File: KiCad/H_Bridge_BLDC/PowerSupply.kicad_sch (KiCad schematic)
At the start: 16 parts, among them J4 12V, Q10 BC33740BU, U2 L7805CV

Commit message: First version
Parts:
- removed C12: 470uF 250V, footprints:CP_Radial_D25.0mm_P10.00mm_and_5mm, symbol Components:470-uF-250V-PK2E471MND2535
- removed R22: 330, Resistor_THT:R_Axial_DIN0207_L6.3mm_D2.5mm_P10.16mm_Horizontal, symbol Device:R
- added D19: 20V 1N5250B, Diode_THT:D_DO-35_SOD27_P10.16mm_Horizontal, symbol Device:D_Zener
- added R12: 10k, Resistor_THT:R_Axial_DIN0207_L6.3mm_D2.5mm_P10.16mm_Horizontal, symbol Device:R
- added R13: 2k2, Resistor_THT:R_Axial_DIN0207_L6.3mm_D2.5mm_P10.16mm_Horizontal, symbol Device:R
- added R14: 1k, Resistor_THT:R_Axial_DIN0207_L6.3mm_D2.5mm_P10.16mm_Horizontal, symbol Device:R
- D18: value 24V / 2W -> ZY24 24V / 2W; footprint (none) -> Diode_THT:D_DO-41_SOD81_P10.16mm_Horizontal; Digikey (none) -> https://www.digikey.nl/short/zdt4nqp0
- Q10: value BC33740BU -> 2N5551; symbol Components:BC33740BU -> Components:2N5551; Digikey https://www.digikey.nl/short/0dchvj3v -> https://www.digikey.nl/short/t592041t
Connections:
- net GNDD: now also Q10.1 (E), R13.2; no longer Q10.3 (E)
- net HALL_ENABLE: now also D10.1 (K), Q10.3 (C); no longer Q10.1 (C)
- net VD: now also D19.1 (K), R12.1
- net at D10.2 (A): now also R12.2
- net at Q10.2 (B): now also R13.1, R14.2
- new net: D19.2 (A), R14.1
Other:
- note added: "Over Voltage detection"
- moved on the sheet: D10, FL1, R11, R40, R41

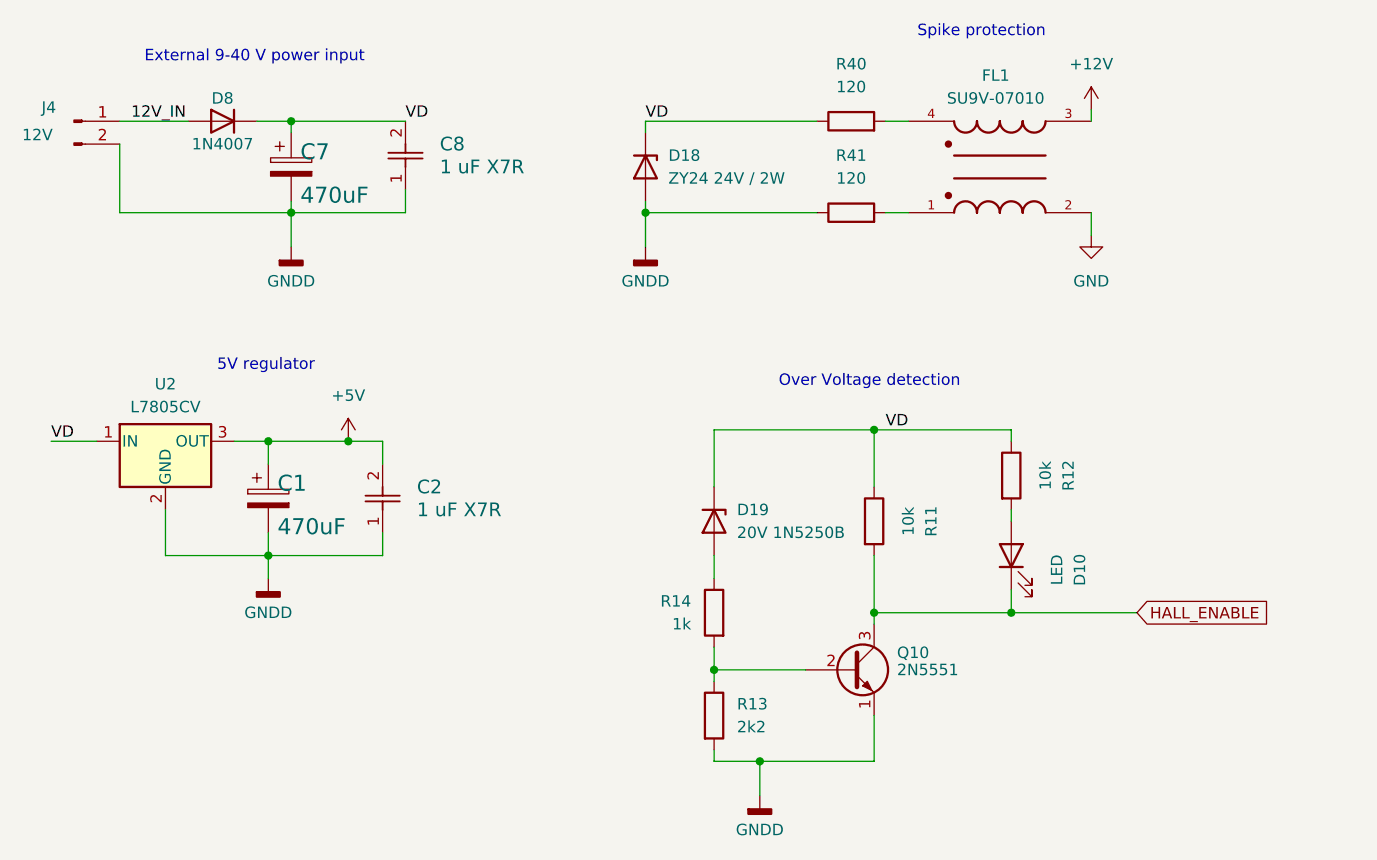
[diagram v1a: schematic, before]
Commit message: Added BOM and changed some parts (same footprint)
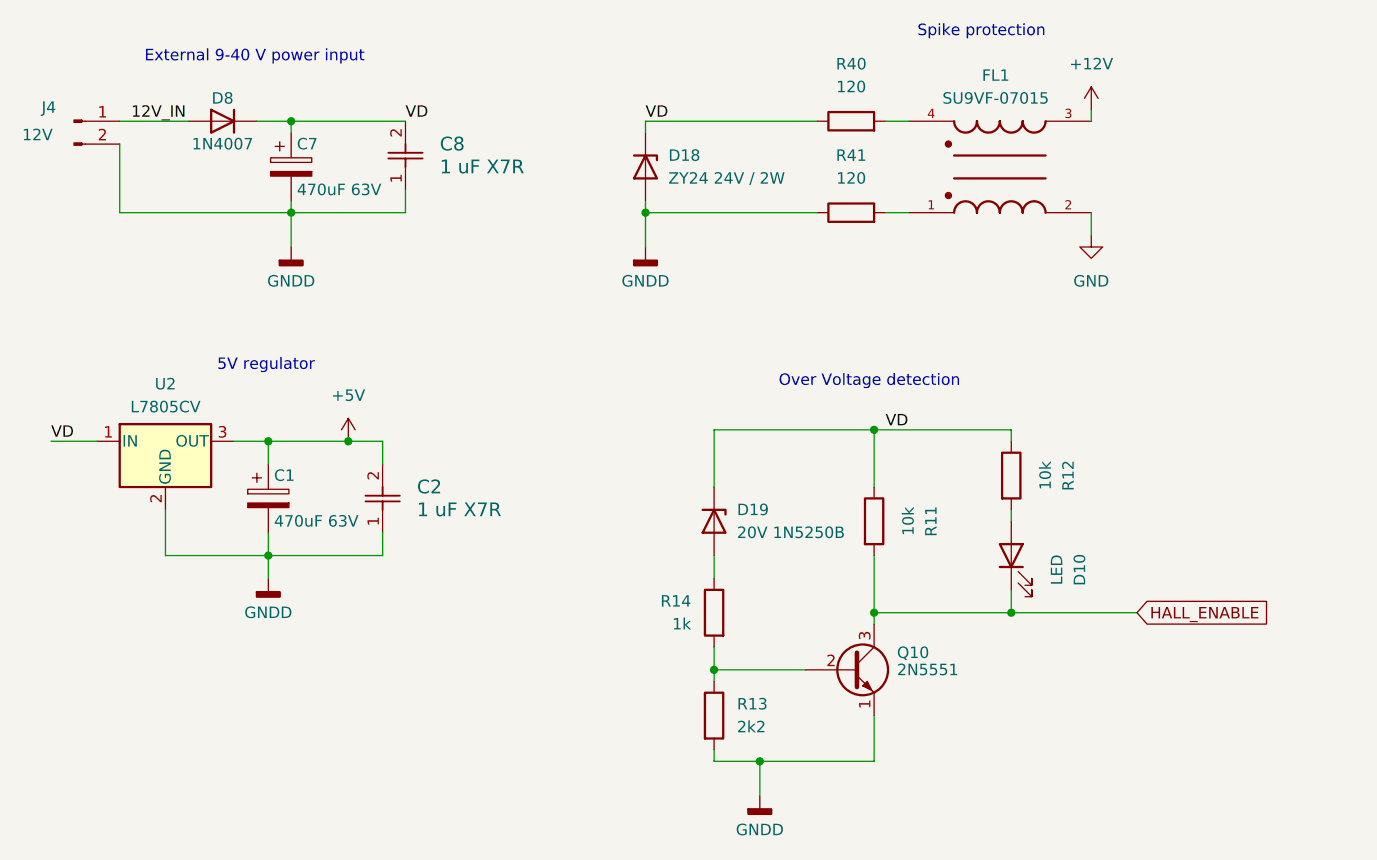
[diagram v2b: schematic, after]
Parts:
- C1, C7: value 470uF -> 470uF 63V; symbol Component_Library:C_Pol_470uF -> Components:470-uF-63V-ESK477M063AL4EA
- FL1: value SU9V-07010 -> SU9VF-07015; Digikey https://www.digikey.nl/short/fbcjc4v0 -> https://www.digikey.nl/short/8qzt38p9
- U2: DigiKey https://www.digikey.nl/short/7nprw4r0 -> (none); Digikey (none) -> https://www.digikey.nl/short/7nprw4r0
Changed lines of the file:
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@@
 			)
 		)
-		(property "Value" "SU9V-07010"
+		(property "Value" "SU9VF-07015"
 			(at 143.0528 41.91 0)
 			(effects
@@
 			)
 		)
-		(property "Description" "1 mH @ 1 kHz 2 Lijn Common Mode Choke Through-hole 700mA DCR 600mOhm"
+		(property "Description" "1.5 mH @ 1 kHz 2 Common Mode Choke Through-hole 700mA"
 			(at 143.51 49.53 0)
 			(effects
@@
 			)
 		)
-		(property "Digikey" "https://www.digikey.nl/short/fbcjc4v0"
+		(property "Digikey" "https://www.digikey.nl/short/8qzt38p9"
 			(at 143.51 49.53 0)
 			(effects
@@
 	)
 	(symbol
-		(lib_id "Component_Library:C_Pol_470uF")
+		(lib_id "Components:470-uF-63V-ESK477M063AL4EA")
 		(at 62.23 86.36 0)
 		(unit 1)
@@
 		(dnp no)
 		(property "Reference" "C1"
-			(at 63.246 85.725 0)
-			(effects
-				(font
-					(size 1.778 1.778)
-				)
-				(justify left bottom)
-			)
-		)
-		(property "Value" "470uF"
-			(at 63.246 90.551 0)
-			(effects
-				(font
-					(size 1.778 1.778)
-				)
-				(justify left bottom)
+			(at 62.865 83.82 0)
+			(effects
+				(font
+					(size 1.27 1.27)
+				)
+				(justify left)
+			)
+		)
+		(property "Value" "470uF 63V"
+			(at 62.865 88.9 0)
+			(effects
+				(font
+					(size 1.27 1.27)
+				)
+				(justify left)
 			)
 		)
@@
 			)
 		)
-		(property "Datasheet" "~"
+		(property "Datasheet" "https://search.kemet.com/download/datasheet/ESK477M063AL4EA"
 			(at 62.23 86.36 0)
 			(effects
@@
 	)
 	(symbol
-		(lib_id "Component_Library:C_Pol_470uF")
+		(lib_id "Components:470-uF-63V-ESK477M063AL4EA")
 		(at 64.77 49.53 0)
 		(unit 1)
@@
 		(dnp no)
 		(property "Reference" "C7"
-			(at 65.786 48.895 0)
-			(effects
-				(font
-					(size 1.778 1.778)
-				)
-				(justify left bottom)
-			)
-		)
-		(property "Value" "470uF"
-			(at 65.786 53.721 0)
-			(effects
-				(font
-					(size 1.778 1.778)
-				)
-				(justify left bottom)
+			(at 65.405 46.99 0)
+			(effects
+				(font
+					(size 1.27 1.27)
+				)
+				(justify left)
+			)
+		)
+		(property "Value" "470uF 63V"
+			(at 65.405 52.07 0)
+			(effects
+				(font
+					(size 1.27 1.27)
+				)
+				(justify left)
 			)
 		)
@@
 			)
 		)
-		(property "Datasheet" "~"
+		(property "Datasheet" "https://search.kemet.com/download/datasheet/ESK477M063AL4EA"
 			(at 64.77 49.53 0)
 			(effects
@@
 			)
 		)
-		(property "DigiKey" "https://www.digikey.nl/short/7nprw4r0"
+		(property "Digikey" "https://www.digikey.nl/short/7nprw4r0"
 			(at 50.8 80.01 0)
 			(effects

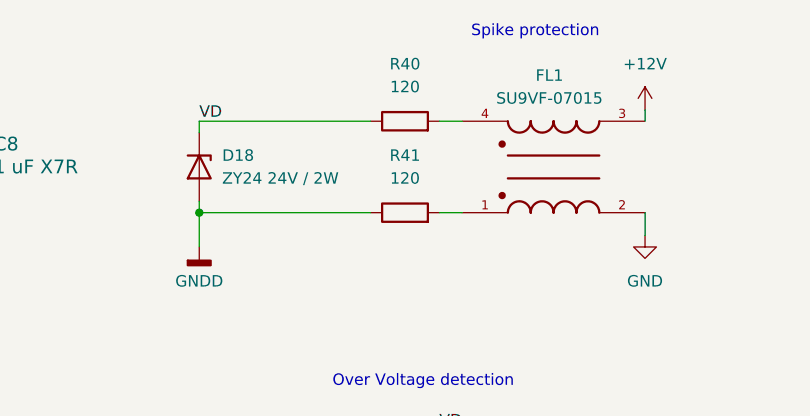
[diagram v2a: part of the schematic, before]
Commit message: Changed a few values and completed BOM.
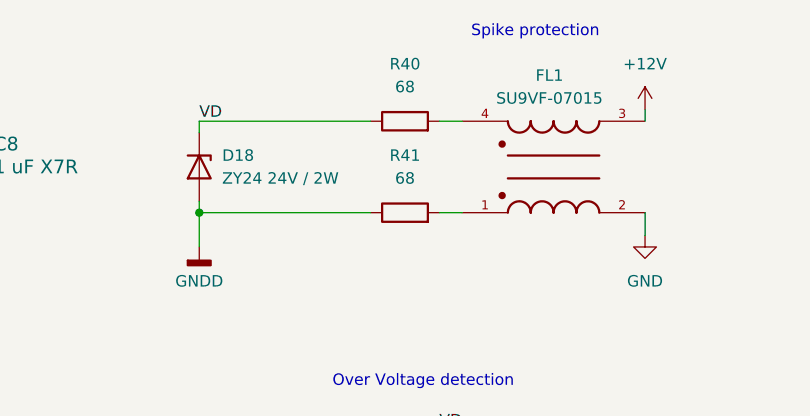
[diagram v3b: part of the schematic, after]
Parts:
- R40, R41: value 120 -> 68
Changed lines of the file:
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@@
 			)
 		)
-		(property "Value" "120"
+		(property "Value" "68"
 			(at 127 40.64 90)
 			(effects
@@
 			)
 		)
-		(property "Value" "120"
+		(property "Value" "68"
 			(at 127 50.8 90)
 			(effects

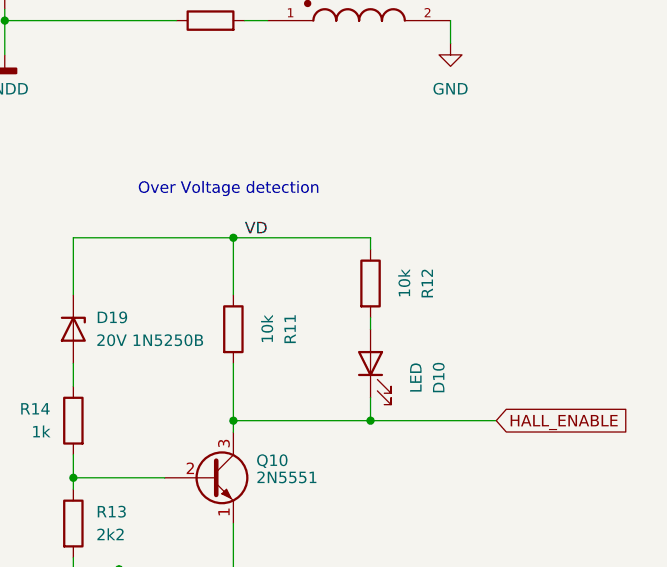
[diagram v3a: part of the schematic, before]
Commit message: Added photograph of prototype PCB with resistors in place.
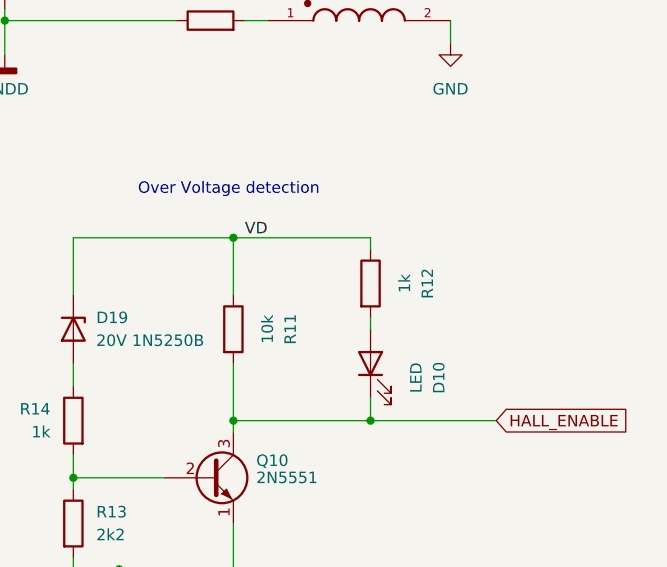
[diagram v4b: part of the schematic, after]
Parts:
- R12: value 10k -> 1k
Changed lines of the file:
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@@
 			)
 		)
-		(property "Value" "10k"
+		(property "Value" "1k"
 			(at 148.59 83.82 90)
 			(effects

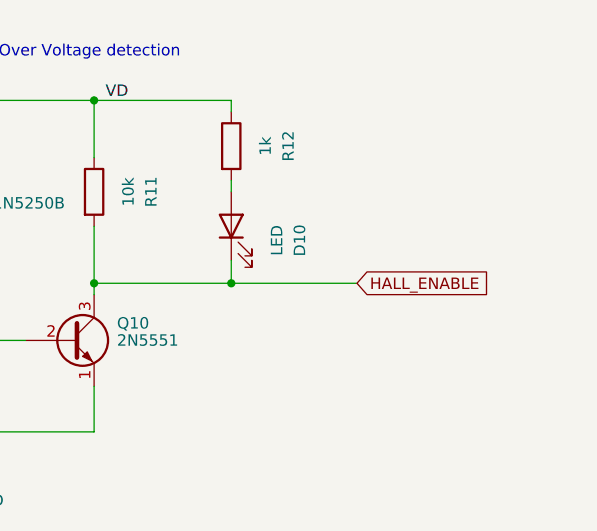
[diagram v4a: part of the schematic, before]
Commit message: Corrected schematic with components that need to be manually added.
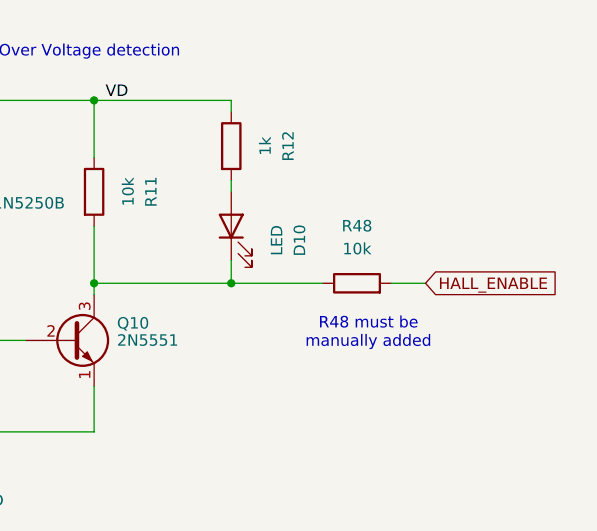
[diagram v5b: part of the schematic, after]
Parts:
- added R48: 10k, Resistor_THT:R_Axial_DIN0207_L6.3mm_D2.5mm_P10.16mm_Horizontal, symbol Device:R
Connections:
- net HALL_ENABLE: now also R48.2; no longer D10.1 (K), Q10.3 (C), R11.2
- new net: D10.1 (K), Q10.3 (C), R11.2, R48.1
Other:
- note added: "R48 must be manually added"
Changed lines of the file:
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@@
+	)
+	(junction
+		(at 64.77 54.61)
+		(diameter 0)
+		(color 0 0 0 0)
+	)
+	(junction
+		(at 129.54 78.74)
+		(diameter 0)
+		(color 0 0 0 0)
+	)
+	(junction
+		(at 116.84 115.57)
+		(diameter 0)
+		(color 0 0 0 0)
+	)
+	(junction
+		(at 62.23 92.71)
+		(diameter 0)
+		(color 0 0 0 0)
 	)
 	(junction
@@
 	)
 	(junction
-		(at 64.77 54.61)
-		(diameter 0)
-		(color 0 0 0 0)
-	)
-	(junction
-		(at 129.54 78.74)
-		(diameter 0)
-		(color 0 0 0 0)
-	)
-	(junction
-		(at 116.84 115.57)
-		(diameter 0)
-		(color 0 0 0 0)
-	)
-	(junction
-		(at 62.23 92.71)
-		(diameter 0)
-		(color 0 0 0 0)
-	)
-	(junction
 		(at 71.12 80.01)
 		(diameter 0)
@@
 	(wire
 		(pts
+			(xy 144.78 99.06) (xy 154.94 99.06)
+		)
+		(stroke
+			(width 0)
+			(type default)
+		)
+	)
+	(wire
+		(pts
 			(xy 62.23 80.01) (xy 71.12 80.01)
 		)
@@
 	(wire
 		(pts
+			(xy 162.56 99.06) (xy 166.37 99.06)
+		)
+		(stroke
+			(width 0)
+			(type default)
+		)
+	)
+	(wire
+		(pts
 			(xy 104.14 44.45) (xy 123.19 44.45)
 		)
@@
 	(wire
 		(pts
-			(xy 144.78 99.06) (xy 158.75 99.06)
-		)
-		(stroke
-			(width 0)
-			(type default)
-		)
-	)
-	(wire
-		(pts
 			(xy 64.77 54.61) (xy 64.77 53.34)
 		)
@@
 		(exclude_from_sim no)
 		(at 129.032 73.406 0)
+		(effects
+			(font
+				(size 1.27 1.27)
+			)
+		)
+	)
+	(text "R48 must be\nmanually added"
+		(exclude_from_sim no)
+		(at 160.02 104.648 0)
 		(effects
 			(font
@@
 	(global_label "HALL_ENABLE"
 		(shape input)
-		(at 158.75 99.06 0)
+		(at 166.37 99.06 0)
 		(fields_autoplaced yes)
 		(effects
@@
 		)
 		(property "Intersheetrefs" "${INTERSHEET_REFS}"
-			(at 174.1933 99.06 0)
+			(at 181.8133 99.06 0)
 			(effects
 				(font
@@
 					(unit 1)
 				)
+			)
+		)
+	)
+	(symbol
+		(lib_id "Device:R")
+		(at 158.75 99.06 90)
+		(unit 1)
+		(exclude_from_sim no)
+		(in_bom yes)
+		(on_board yes)
+		(dnp no)
+		(property "Reference" "R48"
+			(at 158.75 92.71 90)
+			(effects
+				(font
+					(size 1.27 1.27)
+				)
+			)
+		)
+		(property "Value" "10k"
+			(at 158.75 95.25 90)
+			(effects
+				(font
+					(size 1.27 1.27)
+				)
+			)
+		)
+		(property "Footprint" "Resistor_THT:R_Axial_DIN0207_L6.3mm_D2.5mm_P10.16mm_Horizontal"
+			(at 158.75 100.838 90)
+			(effects
+				(font
+					(size 1.27 1.27)
+				)
+				(hide yes)
+			)
+		)
+		(property "Datasheet" "~"
+			(at 158.75 99.06 0)
+			(effects
+				(font
+					(size 1.27 1.27)
+				)
+				(hide yes)
+			)
+		)
+		(property "Description" ""
+			(at 158.75 99.06 0)
+			(effects
+				(font
+					(size 1.27 1.27)
+				)
+				(hide yes)
+			)
+		)
+		(pin "1"
+		)
+		(pin "2"
+		)
+		(instances
+			(project "H_Bridge_BLDC"
+				(path "/aeb68331-6711-40f3-bf75-cc15a682417a/0ee02df5-2d7f-4946-a04b-92c898f0c4eb"
+					(reference "R48")
+					(unit 1)
+				)
